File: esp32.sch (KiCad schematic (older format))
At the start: 21 parts

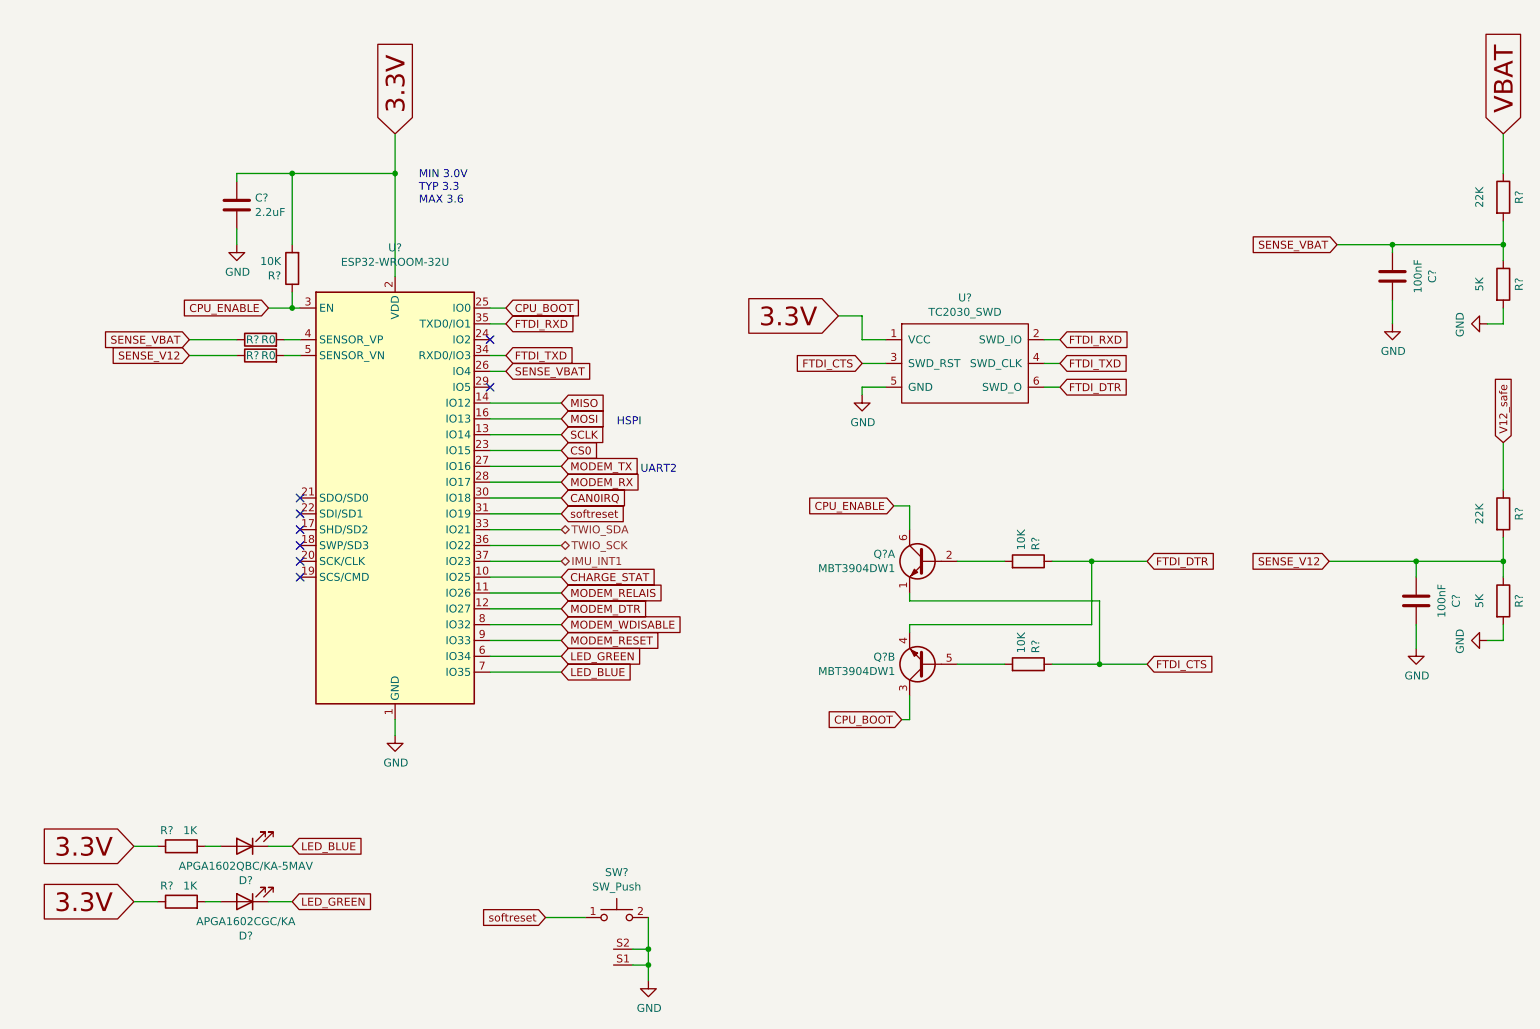
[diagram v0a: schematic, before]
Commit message: Esp32 & Canbus Sch. edited.
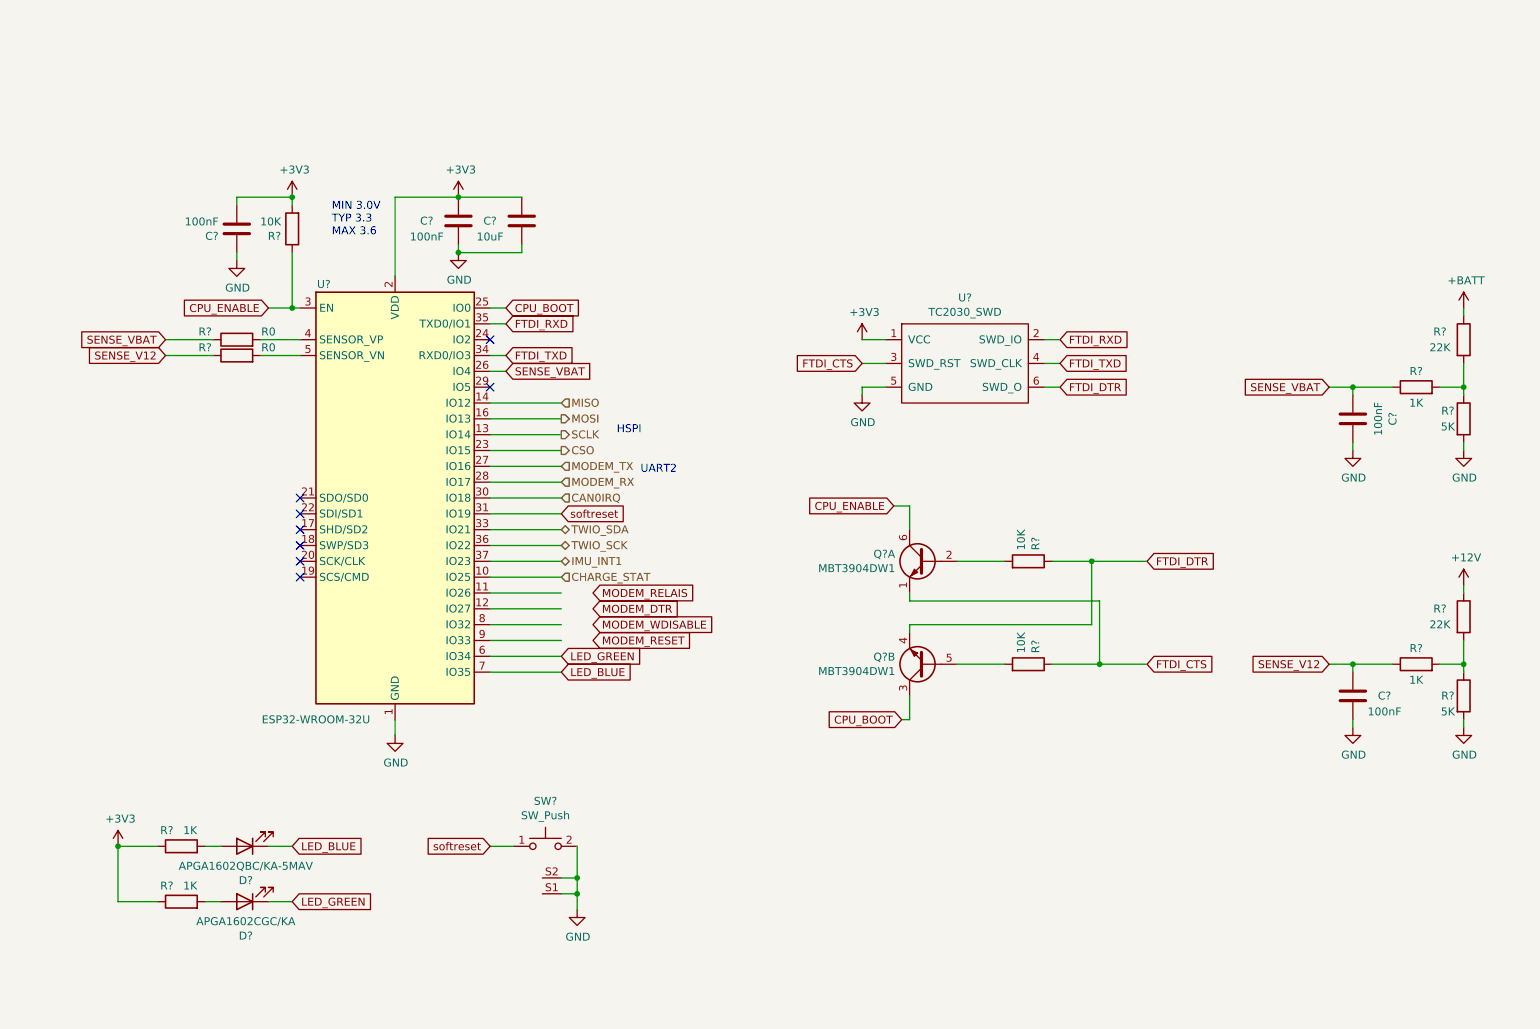
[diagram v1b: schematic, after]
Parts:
- removed C?: 100nF, Capacitor_SMD:C_0603_1608Metric, symbol Device:C
- removed R?: 5K, Resistors:0603, symbol Device:R
- added C? (x2): 100nF, Capacitor_SMD:C_0603_1608Metric, symbol Device:C
- added C?: 10uF, Capacitor_SMD:C_0603_1608Metric, symbol Device:C
- added R? (x2): 1K, Resistors:0603, symbol Device:R
- added R?: 5K, Resistors:0603, symbol Device:R
- C?: value 2.2uF -> 100nF
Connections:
- net labels added: +12V, +3V3, +BATT, CSO
- net labels removed: 3.3V, CS0, V12_safe, VBAT
- wire segments 92 -> 94
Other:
- moved on the sheet: C?, R?, SW?

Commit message: Modem schematic updated.
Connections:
- wire segments 94 -> 95
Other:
- note added: "U2_RXD"
- note added: "U2_TXD"
- note removed: "UART2"
- moved on the sheet: R?
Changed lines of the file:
@@
 $Descr A4 11693 8268
 encoding utf-8
-Sheet 6 6
+Sheet 5 6
 Title ""
 Date ""
@@
 	1    0    0    -1
 $EndComp
-Text GLabel 9400 3100 0    50   Input ~ 0
-SENSE_VBAT
-Text GLabel 9400 4850 0    50   Input ~ 0
-SENSE_V12
 $Comp
 L Device:C C?
@@
 Wire Wire Line
 	2300 6350 2400 6350
-Text GLabel 2850 6350 2    50   Input ~ 0
-LED_GREEN
-Wire Wire Line
-	2850 6350 2700 6350
-Text GLabel 2850 6000 2    50   Input ~ 0
-LED_BLUE
-Wire Wire Line
-	2700 6000 2850 6000
 $Comp
 L aep:SW_Push SW?
@@
 Wire Wire Line
 	6450 2950 6600 2950
-Text GLabel 4750 4700 2    50   Input ~ 0
-MODEM_RESET
-Text GLabel 4750 4500 2    50   Input ~ 0
-MODEM_DTR
-Text GLabel 4750 4600 2    50   Input ~ 0
-MODEM_WDISABLE
 $Comp
 L Device:R R?
 U 1 1 603F64E1
-P 2500 2800
+P 4500 3000
 AR Path="/603F64E1" Ref="R?"  Part="1"
 AR Path="/603B75FA/603F64E1" Ref="R?"  Part="1"
-F 0 "R?" V 2550 3000 50  0000 C CNN
-F 1 "R0" V 2550 2600 50  0000 C CNN
-F 2 "Resistors:0603" V 2430 2800 50  0001 C CNN
-F 3 "~" H 2500 2800 50  0001 C CNN
-	1    2500 2800
-	0    -1   -1   0
-$EndComp
-Text GLabel 4200 3000 2    50   Input ~ 0
-SENSE_VBAT
-Text GLabel 2050 2900 0    50   Input ~ 0
-SENSE_V12
-Text GLabel 4750 4400 2    50   Input ~ 0
-MODEM_RELAIS
+F 0 "R?" V 4550 3200 50  0000 C CNN
+F 1 "R0" V 4550 2800 50  0000 C CNN
+F 2 "Resistors:0603" V 4430 3000 50  0001 C CNN
+F 3 "~" H 4500 3000 50  0001 C CNN
+	1    4500 3000
+	0    1    1    0
+$EndComp
 Text Notes 3100 2150 0    50   ~ 0
 MIN 3.0V\nTYP 3.3\nMAX 3.6
@@
 NoConn ~ 2900 3900
 NoConn ~ 2900 3800
-Text Notes 4900 3400 0    50   ~ 0
+Text Notes 4900 3250 3    50   ~ 0
 HSPI
-Text Notes 5050 3650 0    50   ~ 0
-UART2
+Text Notes 4150 3600 0    50   ~ 0
+U2_RXD
 NoConn ~ 4100 2800
 NoConn ~ 4100 3100
@@
 Wire Wire Line
 	4100 4700 4550 4700
-Wire Wire Line
-	4200 3000 4100 3000
-Text GLabel 2050 2800 0    50   Input ~ 0
-SENSE_VBAT
 $Comp
 L Device:R R?
@@
 	0    -1   -1   0
 $EndComp
-Wire Wire Line
-	2050 2800 2350 2800
-Wire Wire Line
-	2050 2900 2350 2900
 $Comp
 L RF_Module:ESP32-WROOM-32U U?
@@
 Text HLabel 4550 4000 2    50   BiDi ~ 0
 TWIO_SDA
-Text HLabel 4550 4200 2    50   BiDi ~ 0
+Text HLabel 4550 4200 2    50   Input ~ 0
 IMU_INT1
-Text GLabel 4550 4900 2    50   Input ~ 0
-LED_BLUE
-Text GLabel 4550 4800 2    50   Input ~ 0
-LED_GREEN
 $Comp
 L Device:R R?
@@
 Wire Wire Line
 	9800 3100 9550 3100
-Wire Wire Line
-	9400 3100 9550 3100
 Connection ~ 9550 3100
 $Comp
@@
 Wire Wire Line
 	9800 4850 9550 4850
-Wire Wire Line
-	9400 4850 9550 4850
 Connection ~ 9550 4850
 $Comp
@@
 Text HLabel 4550 3600 2    50   Input ~ 0
 MODEM_TX
-Text HLabel 4550 3700 2    50   Input ~ 0
+Text HLabel 4550 3700 2    50   Output ~ 0
 MODEM_RX
 Text HLabel 4550 3800 2    50   Input ~ 0
@@
 Text HLabel 4550 3500 2    50   Output ~ 0
 CSO
+Text Notes 4150 3700 0    50   ~ 0
+U2_TXD
+Text HLabel 4550 4400 2    50   Output ~ 0
+MODEM_RELAIS
+Text HLabel 4550 4500 2    50   Output ~ 0
+MODEM_DTR
+Text HLabel 4550 4600 2    50   Output ~ 0
+MODEM_WDISABLE
+Text HLabel 4550 4700 2    50   Output ~ 0
+MODEM_RESET
+Text Label 4100 4800 0    50   ~ 0
+LED_GREEN
+Text Label 4100 4900 0    50   ~ 0
+LED_BLUE
+Text Label 2850 6000 0    50   ~ 0
+LED_GREEN
+Wire Wire Line
+	2700 6000 3300 6000
+Wire Wire Line
+	2700 6350 3300 6350
+Text Label 2850 6350 0    50   ~ 0
+LED_BLUE
+Text Label 1600 2800 0    50   ~ 0
+SENSE_VBAT
+Wire Wire Line
+	1600 2800 2350 2800
+Text Label 1600 2900 0    50   ~ 0
+SENSE_V12
+Wire Wire Line
+	1600 2900 2350 2900
+Text Label 8950 3100 0    50   ~ 0
+SENSE_VBAT
+Text Label 9000 4850 0    50   ~ 0
+SENSE_V12
+Wire Wire Line
+	8950 3100 9550 3100
+Wire Wire Line
+	9000 4850 9550 4850
+Text Label 4750 3000 0    50   ~ 0
+SENSE_VBAT
+Wire Wire Line
+	4100 3000 4350 3000
+Wire Wire Line
+	4650 3000 5200 3000
 $EndSCHEMATC

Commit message: Power Sch. Updated.
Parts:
- added R22: R0, Resistors:0603, symbol Device:R
- gave numbers to parts that had none: 24
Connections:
- net labels added: CHARGER_EN
- wire segments 95 -> 96
- no-connect marks 8 -> 7
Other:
- moved on the sheet: R25

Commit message: Power section placement completed.
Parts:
- R26: renamed from R22; footprint Resistors:0603 -> Resistor_SMD:R_0603_1608Metric
- R27: renamed from R23; footprint Resistors:0603 -> Resistor_SMD:R_0603_1608Metric
- R28: renamed from R24; footprint Resistors:0603 -> Resistor_SMD:R_0603_1608Metric
- R29: renamed from R25; footprint Resistors:0603 -> Resistor_SMD:R_0603_1608Metric
- R30: renamed from R26; footprint Resistors:0603 -> Resistor_SMD:R_0603_1608Metric
- R31: renamed from R27; footprint Resistors:0603 -> Resistor_SMD:R_0603_1608Metric
- R32: renamed from R28; footprint Resistors:0603 -> Resistor_SMD:R_0603_1608Metric
- R33: renamed from R29; footprint Resistors:0603 -> Resistor_SMD:R_0603_1608Metric
- R34: renamed from R30; footprint Resistors:0603 -> Resistor_SMD:R_0603_1608Metric
- R35: renamed from R31; footprint Resistors:0603 -> Resistor_SMD:R_0603_1608Metric
- R36: renamed from R32; footprint Resistors:0603 -> Resistor_SMD:R_0603_1608Metric
- R37: renamed from R33; footprint Resistors:0603 -> Resistor_SMD:R_0603_1608Metric
- renumbered C40 to C44, C41 to C45, C42 to C46, C43 to C47, C44 to C48, R20 to R24, R21 to R25

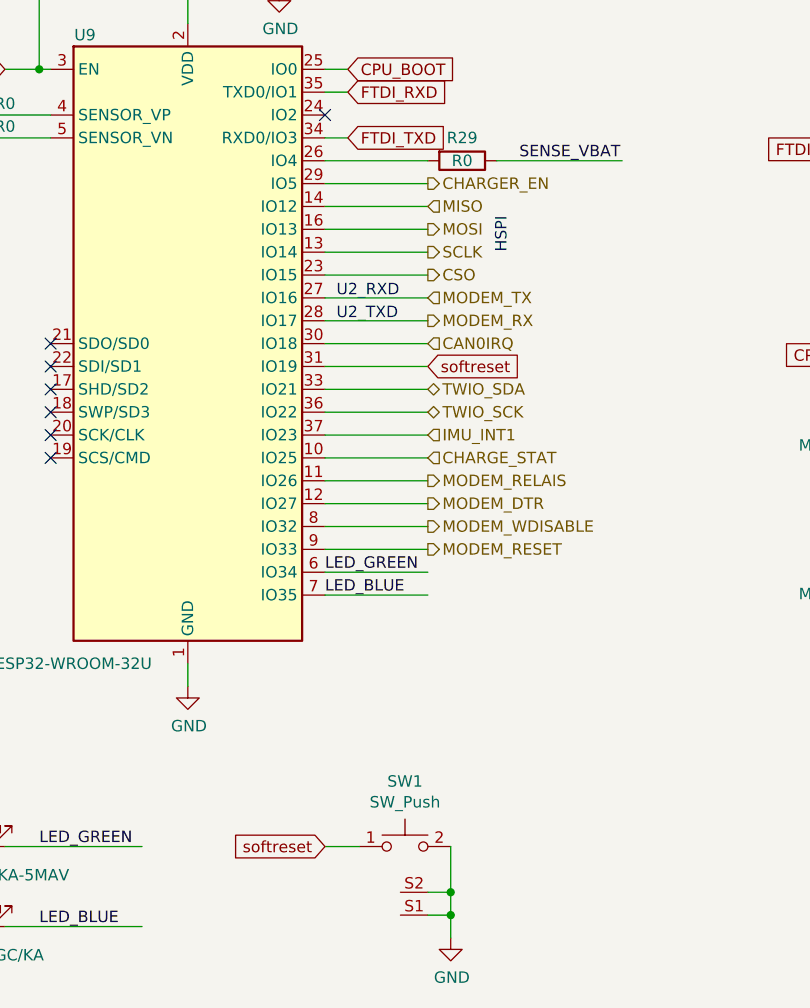
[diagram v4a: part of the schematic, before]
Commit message: Changed MCU connection.
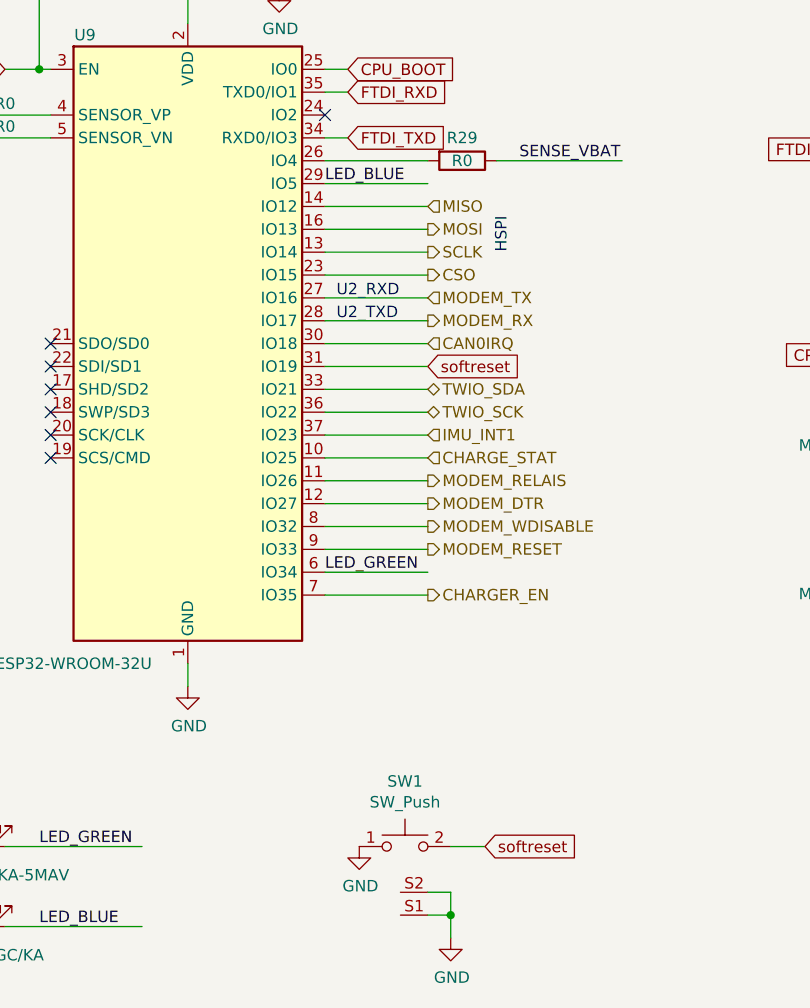
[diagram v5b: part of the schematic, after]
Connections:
- wire segments 96 -> 95
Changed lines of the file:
@@
 $EndComp
-Wire Wire Line
-	4650 6000 4650 6200
 Wire Wire Line
 	4550 6300 4650 6300
@@
 Wire Wire Line
 	4550 6200 4650 6200
-Connection ~ 4650 6200
 Wire Wire Line
 	4650 6200 4650 6300
-Text GLabel 4100 6000 0    50   Input ~ 0
+Text GLabel 4800 6000 2    50   Input ~ 0
 softreset
 $Comp
@@
 	4550 4800 4100 4800
 Wire Wire Line
-	4100 4900 4550 4900
+	4100 3100 4550 3100
 Text HLabel 4550 4100 2    50   BiDi ~ 0
 TWIO_SCK
@@
 CAN0IRQ
 Wire Wire Line
-	4250 6000 4100 6000
+	4650 6000 4800 6000
 Text HLabel 4550 4300 2    50   Input ~ 0
 CHARGE_STAT
@@
 Text Label 4100 4800 0    50   ~ 0
 LED_GREEN
-Text Label 4100 4900 0    50   ~ 0
+Text Label 4100 3100 0    50   ~ 0
 LED_BLUE
 Text Label 2850 6000 0    50   ~ 0
@@
 	0    -1   -1   0
 $EndComp
-Text HLabel 4550 3100 2    50   Output ~ 0
+Text HLabel 4550 4900 2    50   Output ~ 0
 CHARGER_EN
 Wire Wire Line
-	4100 3100 4550 3100
+	4100 4900 4550 4900
 Wire Wire Line
 	4100 3000 4550 3000
+$Comp
+L power:GND #PWR?
+U 1 1 6056CD42
+P 4250 6000
+AR Path="/603D0BBC/6056CD42" Ref="#PWR?"  Part="1"
+AR Path="/6056CD42" Ref="#PWR?"  Part="1"
+AR Path="/603B75FA/6056CD42" Ref="#PWR0101"  Part="1"
+F 0 "#PWR0101" H 4250 5750 50  0001 C CNN
+F 1 "GND" H 4255 5827 50  0000 C CNN
+F 2 "" H 4250 6000 50  0001 C CNN
+F 3 "" H 4250 6000 50  0001 C CNN
+	1    4250 6000
+	1    0    0    -1
+$EndComp
 $EndSCHEMATC
